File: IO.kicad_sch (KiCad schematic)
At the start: 9 parts, among them J10 Conn_01x04_Pin, J2 Conn_01x02_Pin, J3 Conn_01x02_Pin, J4 Conn_01x02_Pin, J5 Conn_01x02_Pin, J6 Conn_01x02_Pin, J7 Conn_01x04_Pin, J8 Conn_01x04_Pin, J9 Conn_01x04_Pin

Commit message: added some notes and PDF
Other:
- moved on the sheet: J10, J7, J8, J9

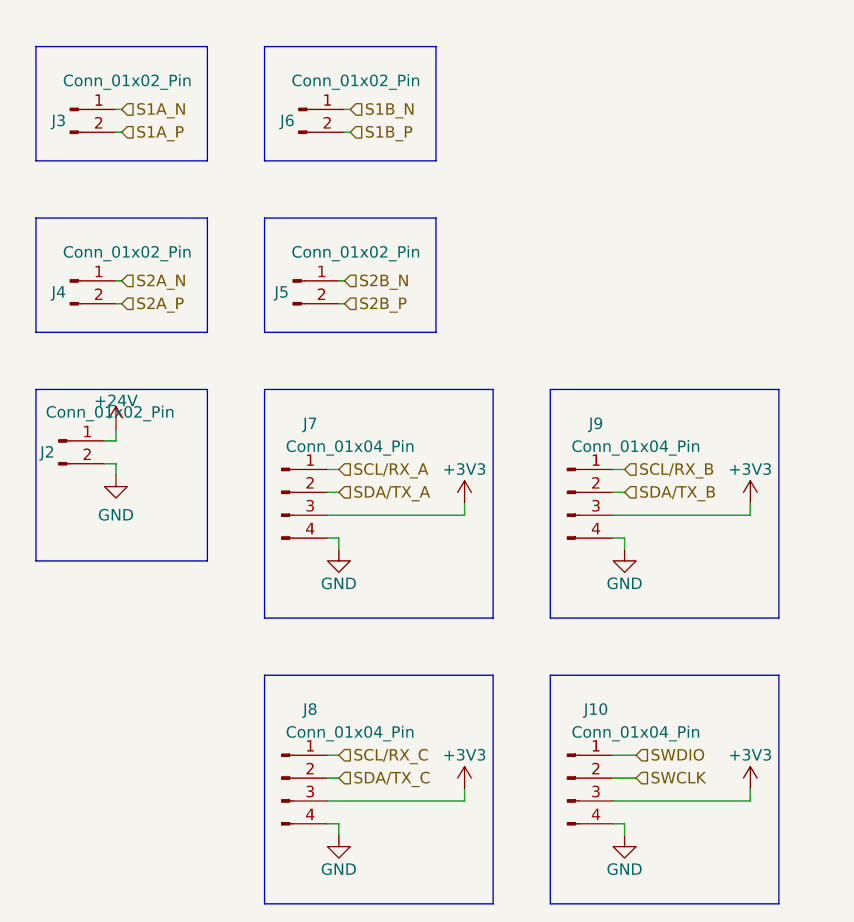
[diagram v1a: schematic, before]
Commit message: started on layout and added SD/flash/BNO
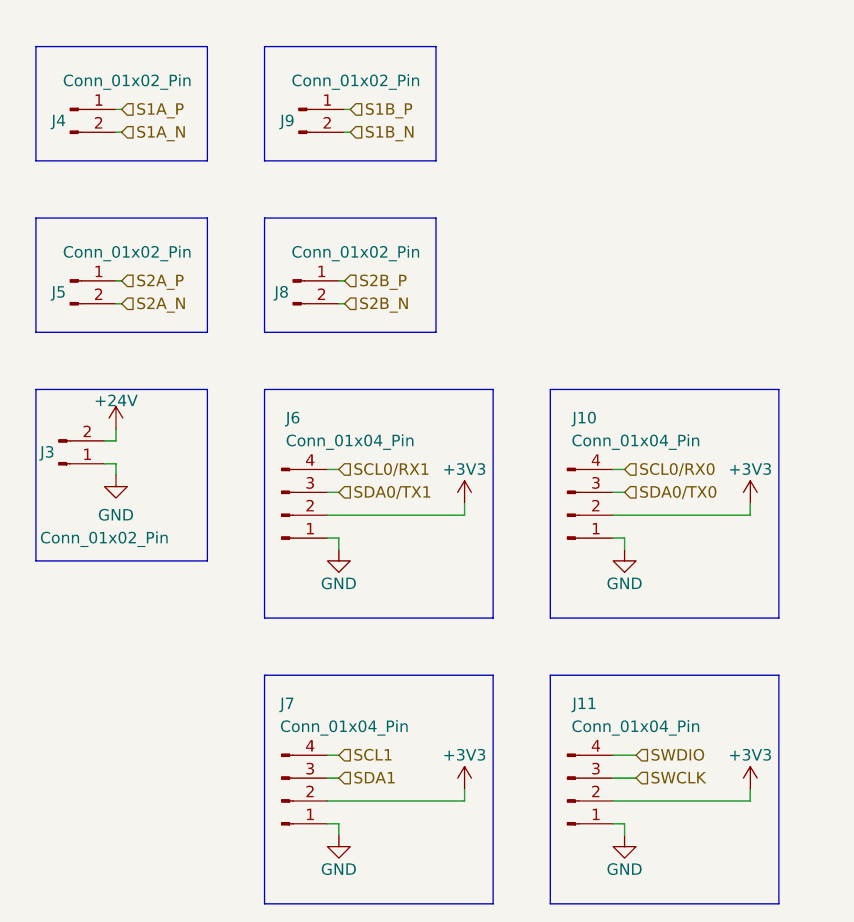
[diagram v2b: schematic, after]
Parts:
- J10: renamed from J9; footprint Connector_Molex:Molex_SL_171971-0004_1x04_P2.54mm_Vertical -> connector_molex_70543:molex_70543-0038_4pin
- J11: renamed from J10; footprint Connector_PinHeader_2.54mm:PinHeader_1x04_P2.54mm_Vertical -> Connector_PinHeader_1.27mm:PinHeader_1x04_P1.27mm_Vertical
- J4: renamed from J3; footprint Connector_Molex:Molex_SL_171971-0002_1x02_P2.54mm_Vertical -> connector_molex_70543:molex_70543-0036_2pin
- J5: renamed from J4; footprint Connector_Molex:Molex_SL_171971-0002_1x02_P2.54mm_Vertical -> connector_molex_70543:molex_70543-0036_2pin
- J6: renamed from J7; footprint Connector_Molex:Molex_SL_171971-0004_1x04_P2.54mm_Vertical -> connector_molex_70543:molex_70543-0038_4pin
- J7: renamed from J8; footprint Connector_Molex:Molex_SL_171971-0004_1x04_P2.54mm_Vertical -> connector_molex_70543:molex_70543-0038_4pin
- J8: renamed from J5; footprint Connector_Molex:Molex_SL_171971-0002_1x02_P2.54mm_Vertical -> connector_molex_70543:molex_70543-0036_2pin
- J9: renamed from J6; footprint Connector_Molex:Molex_SL_171971-0002_1x02_P2.54mm_Vertical -> connector_molex_70543:molex_70543-0036_2pin
- renumbered J2 to J3
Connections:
- net SCL/RX_A is gone; now on net GND: J6.1 (Pin_1)
- net SCL/RX_B is gone; now on net GND: J10.1 (Pin_1)
- net SCL/RX_C is gone; now on net GND: J7.1 (Pin_1)
- net SDA/TX_A is gone; now on net +3V3: J6.2 (Pin_2)
- net SDA/TX_B is gone; now on net +3V3: J10.2 (Pin_2)
- net SDA/TX_C is gone; now on net +3V3: J7.2 (Pin_2)
- net +24V: now also J3.2 (Pin_2); no longer J3.1 (Pin_1)
- net +3V3: now also J11.2 (Pin_2); no longer J10.3 (Pin_3), J11.3 (Pin_3), J6.3 (Pin_3), J7.3 (Pin_3)
- net GND: now also J11.1 (Pin_1), J3.1 (Pin_1); no longer J10.4 (Pin_4), J11.4 (Pin_4), J3.2 (Pin_2), J6.4 (Pin_4), J7.4 (Pin_4)
- net S1A_N: now also J4.2 (Pin_2); no longer J4.1 (Pin_1)
- net S1A_P: now also J4.1 (Pin_1); no longer J4.2 (Pin_2)
- net S1B_N: now also J9.2 (Pin_2); no longer J9.1 (Pin_1)
- net S1B_P: now also J9.1 (Pin_1); no longer J9.2 (Pin_2)
- net S2A_N: now also J5.2 (Pin_2); no longer J5.1 (Pin_1)
- net S2A_P: now also J5.1 (Pin_1); no longer J5.2 (Pin_2)
- net S2B_N: now also J8.2 (Pin_2); no longer J8.1 (Pin_1)
- net S2B_P: now also J8.1 (Pin_1); no longer J8.2 (Pin_2)
- net SWCLK: now also J11.3 (Pin_3); no longer J11.2 (Pin_2)
- net SWDIO: now also J11.4 (Pin_4); no longer J11.1 (Pin_1)
- new net SCL0/RX0: J10.4 (Pin_4)
- new net SCL0/RX1: J6.4 (Pin_4)
- new net SCL1: J7.4 (Pin_4)
- new net SDA0/TX0: J10.3 (Pin_3)
- new net SDA0/TX1: J6.3 (Pin_3)
- new net SDA1: J7.3 (Pin_3)

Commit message: final
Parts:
- removed J4, J5, J8, J9: Conn_01x02_Pin, connector_molex_70543:molex_70543-0036_2pin, symbol Connector:Conn_01x02_Pin
- added J10, J5, J6, J9: Conn_01x03, Connector_PinHeader_2.54mm:PinHeader_1x03_P2.54mm_Horizontal, symbol Connector_Generic:Conn_01x03
- renumbered J10 to J11, J11 to J12, J3 to J4, J6 to J7, J7 to J8
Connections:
- net GND: now also J10.3 (Pin_3), J5.3 (Pin_3), J6.3 (Pin_3), J9.3 (Pin_3)
- new net S1A: J5.1 (Pin_1)
- new net S1B: J9.1 (Pin_1)
- new net S2A: J6.1 (Pin_1)
- new net S2B: J10.1 (Pin_1)
- new net SPWR_A: J5.2 (Pin_2), J6.2 (Pin_2)
- new net SPWR_B: J10.2 (Pin_2), J9.2 (Pin_2)
